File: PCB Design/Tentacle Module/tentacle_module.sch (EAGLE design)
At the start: 49 parts, among them IC1 5V, T1 NTD5867NL, T2 NTD5867NL, T3 NTD5867NL, T4 NTD5867NL, X3 RJ45-8X, X4 RJ45-8X

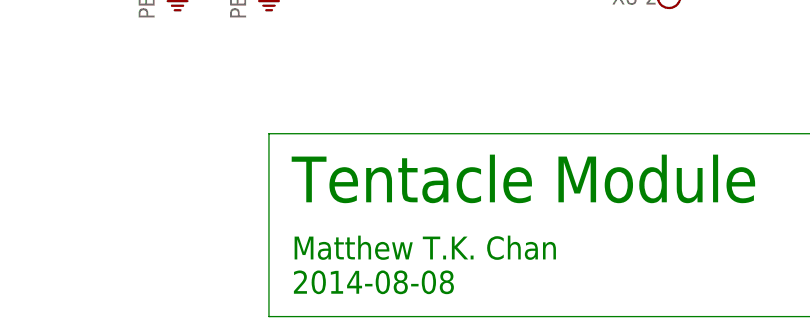
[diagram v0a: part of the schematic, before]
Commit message: Added the RJ45 connector
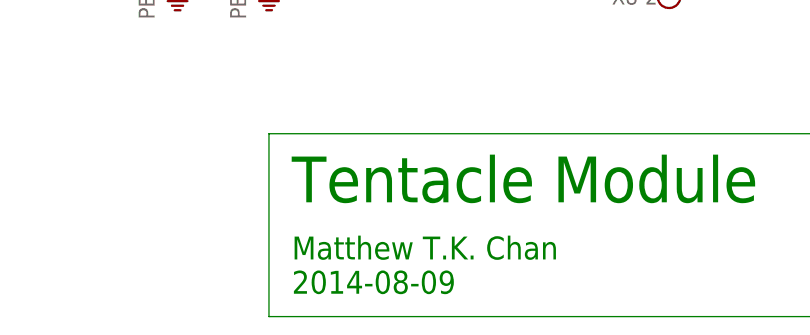
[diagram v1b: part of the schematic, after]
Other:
- note added: "Matthew T.K. Chan 2014-08-09"
- note removed: "Matthew T.K. Chan 2014-08-08"
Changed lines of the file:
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@@
 <text x="198.12" y="20.32" size="5.08" layer="91">Tentacle Module</text>
 <text x="198.12" y="10.16" size="2.54" layer="91">Matthew T.K. Chan
-2014-08-08</text>
+2014-08-09</text>
 <text x="15.24" y="124.46" size="1.778" layer="91">+12V supply headers
     * for attachment of polarized headers

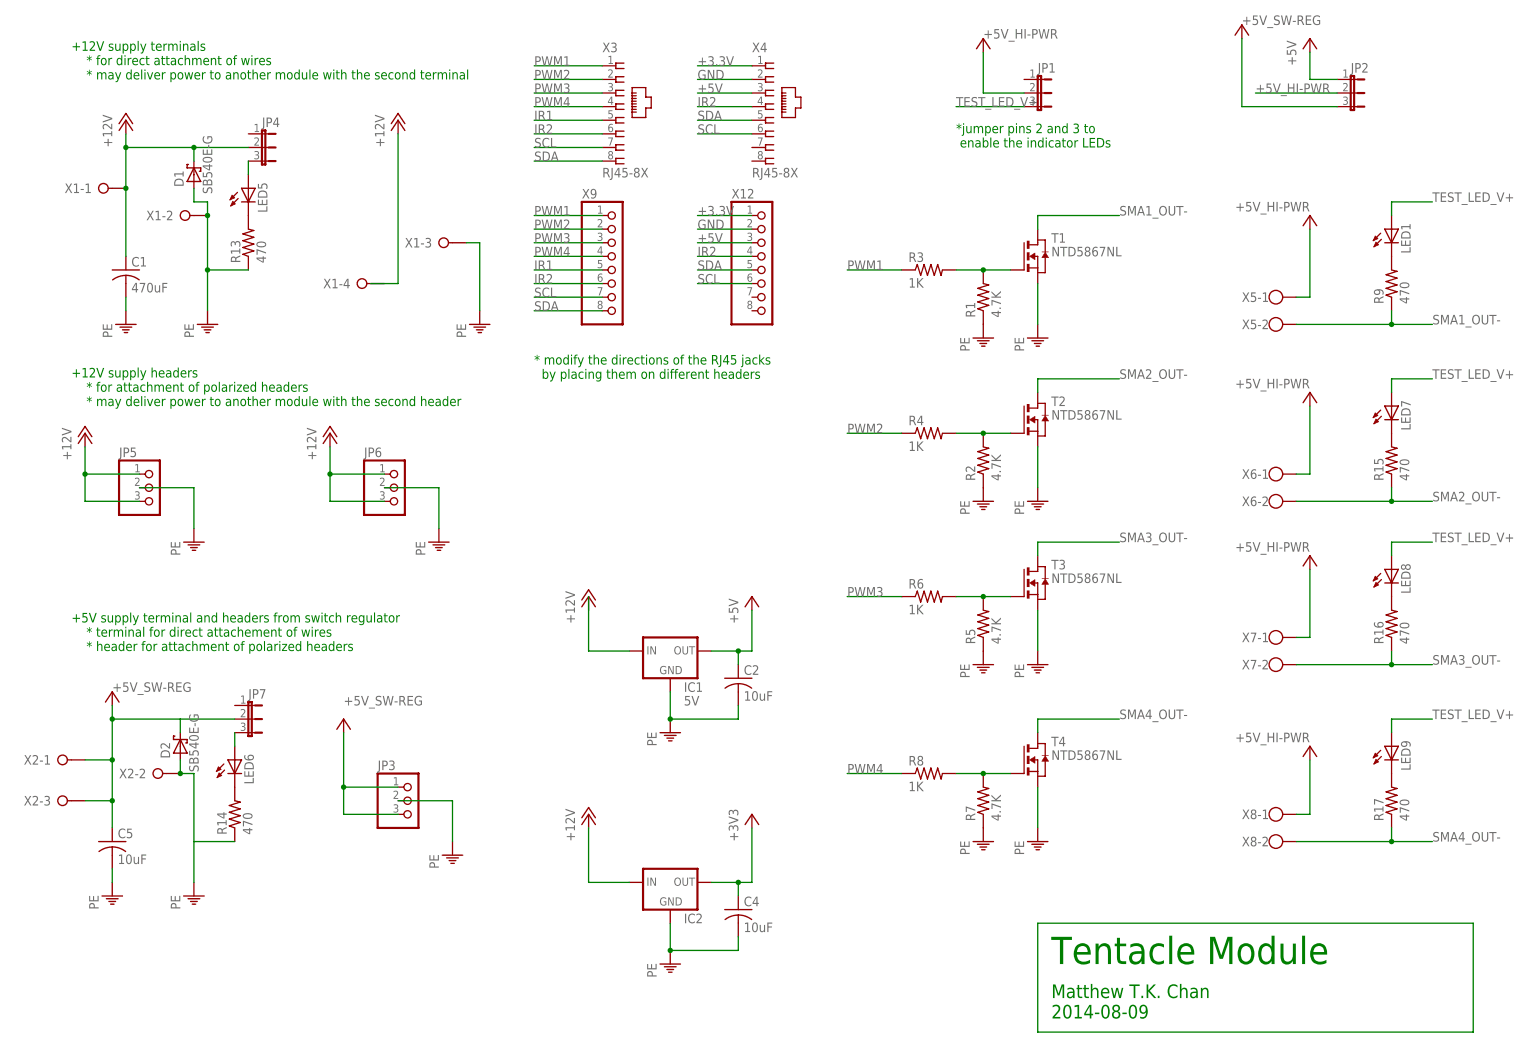
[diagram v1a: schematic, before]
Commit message: Routed the RJ45 connector with side and top headers
Also added the accelerometer chip to the library
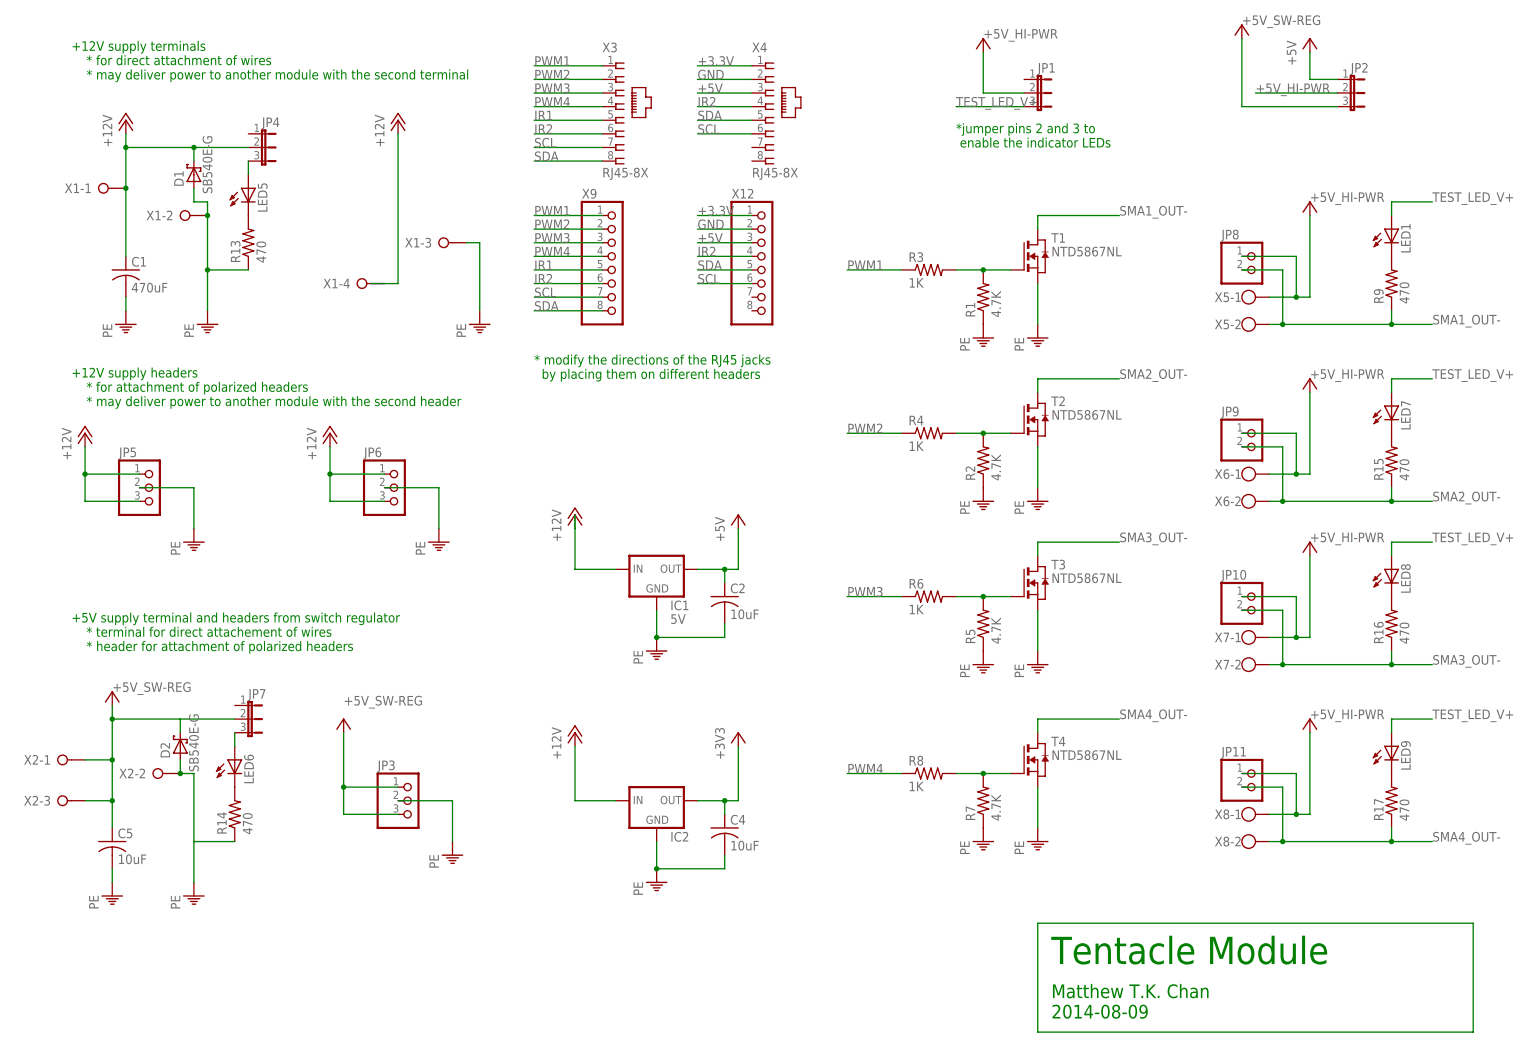
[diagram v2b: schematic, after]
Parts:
- added JP10, JP11, JP8, JP9: (no value), CBLA_Test_bed_Library:PINHD-1X2/90
- JP3, JP5, JP6: device pinhead:PINHD-1X3/90 -> CBLA_Test_bed_Library:PINHD-1X3/90
- X12, X9: device pinhead:PINHD-1X8/90 -> CBLA_Test_bed_Library:PINHD-1X8/90
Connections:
- net +5V_HI-PWR: now also JP10.1, JP11.1, JP8.1, JP9.1
- net SMA1_OUT-: now also JP8.2
- net SMA2_OUT-: now also JP9.2
- net SMA3_OUT-: now also JP10.2
- net SMA4_OUT-: now also JP11.2
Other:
- moved on the sheet: C2, C4, IC1, IC2, X5-1, X5-2, X6-1, X6-2, X7-1, X7-2, X8-1, X8-2

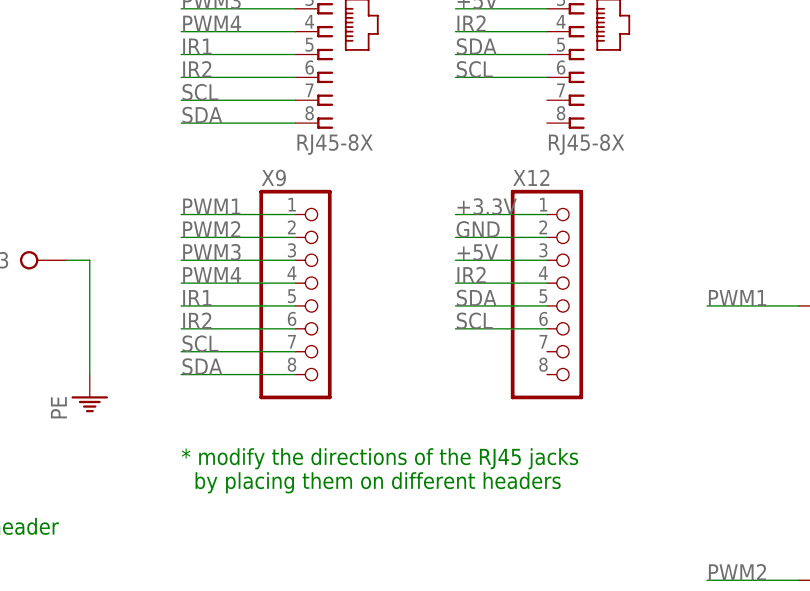
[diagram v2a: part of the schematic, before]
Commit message: Changed location of the header to make it much easier to router
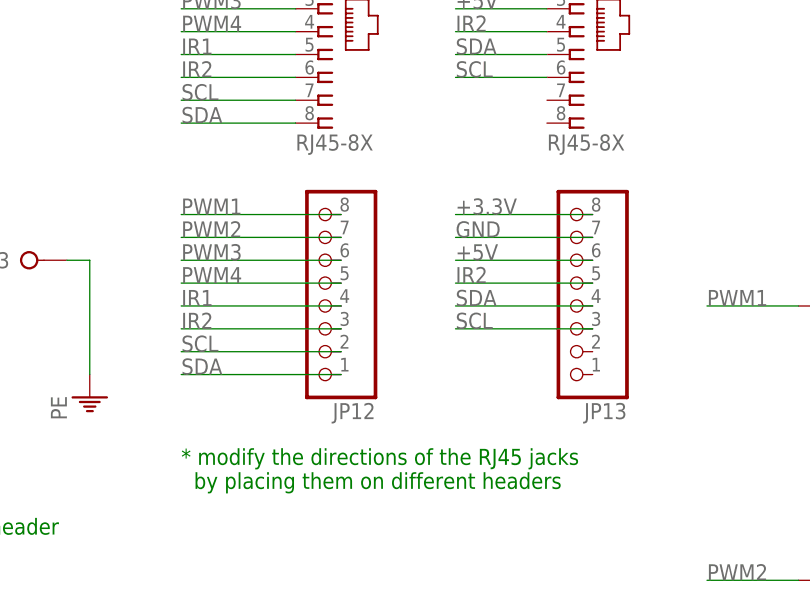
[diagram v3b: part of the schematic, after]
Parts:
- removed X12, X9: (no value), CBLA_Test_bed_Library:PINHD-1X8/90
- added JP12, JP13: (no value), CBLA_Test_bed_Library:PINHD-1X8/90
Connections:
- net +3.3V: now also JP13.8; no longer X12.1
- net +5V: now also JP13.6; no longer X12.3
- net GND: now also JP13.7; no longer X12.2
- net IR1: now also JP12.4; no longer X9.5
- net IR2: now also JP12.3, JP13.5; no longer X12.4, X9.6
- net PWM1: now also JP12.8; no longer X9.1
- net PWM2: now also JP12.7; no longer X9.2
- net PWM3: now also JP12.6; no longer X9.3
- net PWM4: now also JP12.5; no longer X9.4
- net SCL: now also JP12.2, JP13.3; no longer X12.6, X9.7
- net SDA: now also JP12.1, JP13.4; no longer X12.5, X9.8
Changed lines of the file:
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@@
 <part name="P+16" library="supply1" deviceset="+12V" device=""/>
 <part name="P+11" library="supply1" deviceset="+5V" device="" value="+5V_HI-PWR"/>
-<part name="X9" library="CBLA_Test_bed_Library" deviceset="PINHD-1X8" device="/90"/>
-<part name="X12" library="CBLA_Test_bed_Library" deviceset="PINHD-1X8" device="/90"/>
 <part name="D1" library="CBLA_Test_bed_Library" deviceset="SB540E-G" device=""/>
 <part name="LED5" library="led" deviceset="LED" device="SML1206"/>
@@
 <part name="JP10" library="CBLA_Test_bed_Library" deviceset="PINHD-1X2" device="/90"/>
 <part name="JP11" library="CBLA_Test_bed_Library" deviceset="PINHD-1X2" device="/90"/>
+<part name="JP12" library="CBLA_Test_bed_Library" deviceset="PINHD-1X8" device="/90"/>
+<part name="JP13" library="CBLA_Test_bed_Library" deviceset="PINHD-1X8" device="/90"/>
 </parts>
 <sheets>
@@
 <attribute name="VALUE" x="185.42" y="193.04" size="1.778" layer="96"/>
 </instance>
-<instance part="X9" gate="A" x="116.84" y="149.86"/>
-<instance part="X12" gate="A" x="144.78" y="149.86"/>
 <instance part="D1" gate="G$1" x="38.1" y="167.64" smashed="yes" rot="R90">
 <attribute name="NAME" x="36.195" y="165.354" size="1.778" layer="95" rot="R90"/>
@@
 <instance part="JP10" gate="G$1" x="236.22" y="86.36"/>
 <instance part="JP11" gate="G$1" x="236.22" y="53.34"/>
+<instance part="JP12" gate="A" x="116.84" y="152.4" rot="R180"/>
+<instance part="JP13" gate="A" x="144.78" y="152.4" rot="R180"/>
 </instances>
 <busses>
@@
 </segment>
 <segment>
-<pinref part="X12" gate="A" pin="3"/>
-<wire x1="142.24" y1="154.94" x2="132.08" y2="154.94" width="0.1524" layer="91"/>
+<wire x1="147.32" y1="154.94" x2="132.08" y2="154.94" width="0.1524" layer="91"/>
 <label x="132.08" y="154.94" size="1.778" layer="95"/>
+<pinref part="JP13" gate="A" pin="6"/>
 </segment>
 </net>
@@
 </segment>
 <segment>
-<pinref part="X9" gate="A" pin="1"/>
-<wire x1="114.3" y1="160.02" x2="101.6" y2="160.02" width="0.1524" layer="91"/>
+<wire x1="119.38" y1="160.02" x2="101.6" y2="160.02" width="0.1524" layer="91"/>
 <label x="101.6" y="160.02" size="1.778" layer="95"/>
+<pinref part="JP12" gate="A" pin="8"/>
 </segment>
 </net>
@@
 </segment>
 <segment>
-<pinref part="X9" gate="A" pin="2"/>
-<wire x1="114.3" y1="157.48" x2="101.6" y2="157.48" width="0.1524" layer="91"/>
+<wire x1="119.38" y1="157.48" x2="101.6" y2="157.48" width="0.1524" layer="91"/>
 <label x="101.6" y="157.48" size="1.778" layer="95"/>
+<pinref part="JP12" gate="A" pin="7"/>
 </segment>
 </net>
@@
 </segment>
 <segment>
-<pinref part="X9" gate="A" pin="3"/>
-<wire x1="114.3" y1="154.94" x2="101.6" y2="154.94" width="0.1524" layer="91"/>
+<wire x1="119.38" y1="154.94" x2="101.6" y2="154.94" width="0.1524" layer="91"/>
 <label x="101.6" y="154.94" size="1.778" layer="95"/>
+<pinref part="JP12" gate="A" pin="6"/>
 </segment>
 <segment>
@@
 </segment>
 <segment>
-<pinref part="X9" gate="A" pin="4"/>
-<wire x1="114.3" y1="152.4" x2="101.6" y2="152.4" width="0.1524" layer="91"/>
+<wire x1="119.38" y1="152.4" x2="101.6" y2="152.4" width="0.1524" layer="91"/>
 <label x="101.6" y="152.4" size="1.778" layer="95"/>
+<pinref part="JP12" gate="A" pin="5"/>
 </segment>
 <segment>
@@
 </segment>
 <segment>
-<pinref part="X9" gate="A" pin="5"/>
-<wire x1="114.3" y1="149.86" x2="101.6" y2="149.86" width="0.1524" layer="91"/>
+<wire x1="119.38" y1="149.86" x2="101.6" y2="149.86" width="0.1524" layer="91"/>
 <label x="101.6" y="149.86" size="1.778" layer="95"/>
+<pinref part="JP12" gate="A" pin="4"/>
 </segment>
 </net>
@@
 </segment>
 <segment>
-<pinref part="X9" gate="A" pin="6"/>
-<wire x1="114.3" y1="147.32" x2="101.6" y2="147.32" width="0.1524" layer="91"/>
+<wire x1="119.38" y1="147.32" x2="101.6" y2="147.32" width="0.1524" layer="91"/>
 <label x="101.6" y="147.32" size="1.778" layer="95"/>
-</segment>
-<segment>
-<pinref part="X12" gate="A" pin="4"/>
-<wire x1="142.24" y1="152.4" x2="132.08" y2="152.4" width="0.1524" layer="91"/>
+<pinref part="JP12" gate="A" pin="3"/>
+</segment>
+<segment>
+<wire x1="147.32" y1="152.4" x2="132.08" y2="152.4" width="0.1524" layer="91"/>
 <label x="132.08" y="152.4" size="1.778" layer="95"/>
+<pinref part="JP13" gate="A" pin="5"/>
 </segment>
 </net>
@@
 </segment>
 <segment>
-<pinref part="X9" gate="A" pin="7"/>
-<wire x1="114.3" y1="144.78" x2="101.6" y2="144.78" width="0.1524" layer="91"/>
+<wire x1="119.38" y1="144.78" x2="101.6" y2="144.78" width="0.1524" layer="91"/>
 <label x="101.6" y="144.78" size="1.778" layer="95"/>
-</segment>
-<segment>
-<pinref part="X12" gate="A" pin="6"/>
-<wire x1="142.24" y1="147.32" x2="132.08" y2="147.32" width="0.1524" layer="91"/>
+<pinref part="JP12" gate="A" pin="2"/>
+</segment>
+<segment>
+<wire x1="147.32" y1="147.32" x2="132.08" y2="147.32" width="0.1524" layer="91"/>
 <label x="132.08" y="147.32" size="1.778" layer="95"/>
+<pinref part="JP13" gate="A" pin="3"/>
 </segment>
 </net>
@@
 </segment>
 <segment>
-<pinref part="X9" gate="A" pin="8"/>
-<wire x1="114.3" y1="142.24" x2="101.6" y2="142.24" width="0.1524" layer="91"/>
+<wire x1="119.38" y1="142.24" x2="101.6" y2="142.24" width="0.1524" layer="91"/>
 <label x="101.6" y="142.24" size="1.778" layer="95"/>
-</segment>
-<segment>
-<pinref part="X12" gate="A" pin="5"/>
-<wire x1="142.24" y1="149.86" x2="132.08" y2="149.86" width="0.1524" layer="91"/>
+<pinref part="JP12" gate="A" pin="1"/>
+</segment>
+<segment>
+<wire x1="147.32" y1="149.86" x2="132.08" y2="149.86" width="0.1524" layer="91"/>
 <label x="132.08" y="149.86" size="1.778" layer="95"/>
+<pinref part="JP13" gate="A" pin="4"/>
 </segment>
 </net>
@@
 </segment>
 <segment>
-<pinref part="X12" gate="A" pin="1"/>
-<wire x1="142.24" y1="160.02" x2="132.08" y2="160.02" width="0.1524" layer="91"/>
+<wire x1="147.32" y1="160.02" x2="132.08" y2="160.02" width="0.1524" layer="91"/>
 <label x="132.08" y="160.02" size="1.778" layer="95"/>
+<pinref part="JP13" gate="A" pin="8"/>
 </segment>
 </net>
@@
 </segment>
 <segment>
-<pinref part="X12" gate="A" pin="2"/>
-<wire x1="142.24" y1="157.48" x2="132.08" y2="157.48" width="0.1524" layer="91"/>
+<wire x1="147.32" y1="157.48" x2="132.08" y2="157.48" width="0.1524" layer="91"/>
 <label x="132.08" y="157.48" size="1.778" layer="95"/>
-</segment>
-</net>
+<pinref part="JP13" gate="A" pin="7"/>
+</segment>
+</net>
